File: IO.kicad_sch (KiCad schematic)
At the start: 17 parts, among them J701 Conn_01x02, J702 Raspberry_Pi_2_3

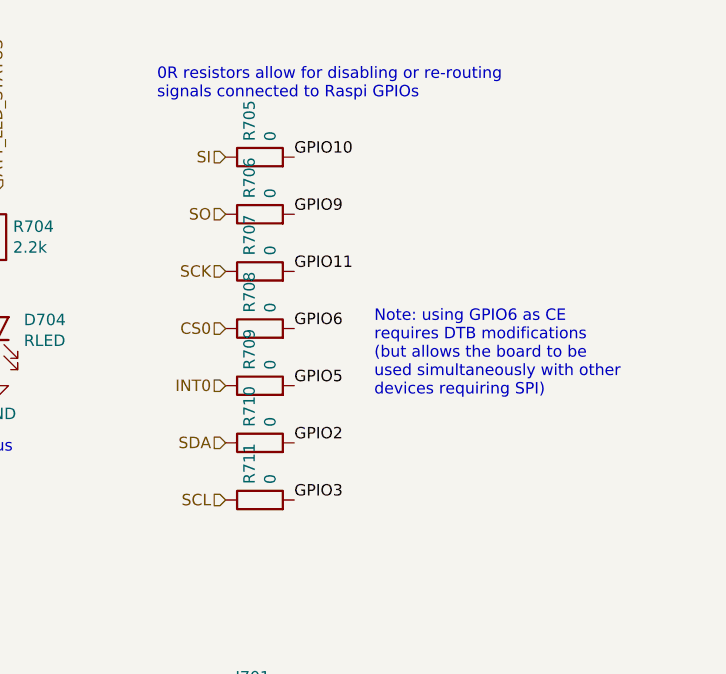
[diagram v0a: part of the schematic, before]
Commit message: Change the power supply topology
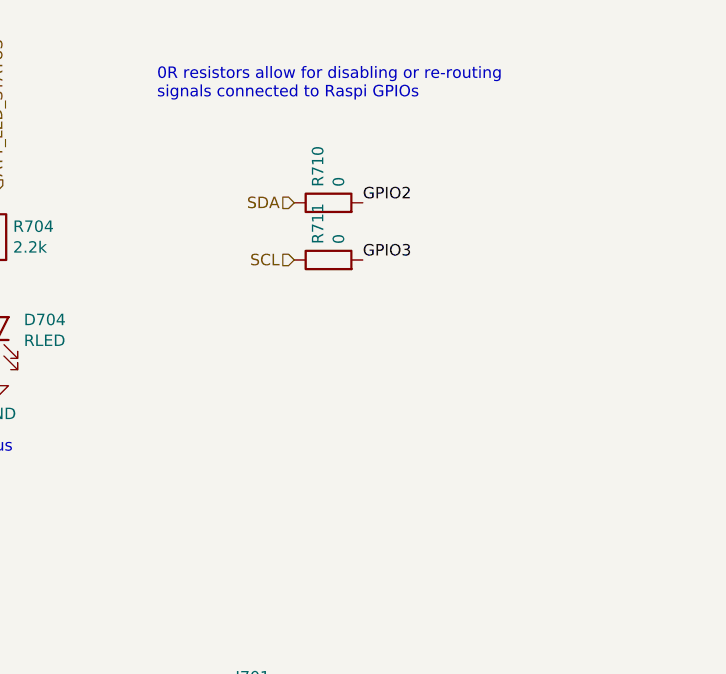
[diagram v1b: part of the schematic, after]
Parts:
- removed R705, R706, R707, R708, R709: 0, Resistor_SMD:R_0603_1608Metric, symbol Device:R
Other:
- note removed: "Note: using GPIO6 as CE requires DTB modifications (but allows the board to be used simultaneously with other devices requiring SPI)"
- moved on the sheet: R710, R711
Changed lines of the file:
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@@
-    (effects (font (size 1.27 1.27)) (justify left bottom))
-  )
-  (text "Note: using GPIO6 as CE\nrequires DTB modifications\n(but allows the board to be \nused simultaneously with other\ndevices requiring SPI)"
-    (at 184.15 63.5 0)
     (effects (font (size 1.27 1.27)) (justify left bottom))
   )
@@
     (effects (font (size 1.27 1.27)) (justify left bottom))
   )
-  (label "GPIO3" (at 175.26 74.93 0)
-    (effects (font (size 1.27 1.27)) (justify left bottom))
-  )
-  (label "GPIO6" (at 175.26 55.88 0)
-    (effects (font (size 1.27 1.27)) (justify left bottom))
-  )
-  (label "GPIO11" (at 175.26 49.53 0)
-    (effects (font (size 1.27 1.27)) (justify left bottom))
-  )
-  (label "GPIO5" (at 175.26 62.23 0)
+  (label "GPIO3" (at 182.88 48.26 0)
     (effects (font (size 1.27 1.27)) (justify left bottom))
   )
@@
     (effects (font (size 1.27 1.27)) (justify left bottom))
   )
-  (label "GPIO2" (at 175.26 68.58 0)
-    (effects (font (size 1.27 1.27)) (justify left bottom))
-  )
-  (label "GPIO9" (at 175.26 43.18 0)
-    (effects (font (size 1.27 1.27)) (justify left bottom))
-  )
-  (label "GPIO10" (at 175.26 36.83 0)
+  (label "GPIO2" (at 182.88 41.91 0)
     (effects (font (size 1.27 1.27)) (justify left bottom))
   )
@@
     (effects (font (size 1.27 1.27)) (justify left))
   )
-  (hierarchical_label "INT0" (shape input) (at 167.64 62.23 180)
-    (effects (font (size 1.27 1.27)) (justify right))
-  )
-  (hierarchical_label "SO" (shape input) (at 167.64 43.18 180)
-    (effects (font (size 1.27 1.27)) (justify right))
-  )
-  (hierarchical_label "SCL" (shape input) (at 167.64 74.93 180)
-    (effects (font (size 1.27 1.27)) (justify right))
-  )
-  (hierarchical_label "SI" (shape input) (at 167.64 36.83 180)
-    (effects (font (size 1.27 1.27)) (justify right))
-  )
-  (hierarchical_label "CS0" (shape input) (at 167.64 55.88 180)
+  (hierarchical_label "SCL" (shape input) (at 175.26 48.26 180)
     (effects (font (size 1.27 1.27)) (justify right))
   )
@@
     (effects (font (size 1.27 1.27)) (justify left))
   )
-  (hierarchical_label "SCK" (shape input) (at 167.64 49.53 180)
-    (effects (font (size 1.27 1.27)) (justify right))
-  )
-  (hierarchical_label "SDA" (shape input) (at 167.64 68.58 180)
+  (hierarchical_label "SDA" (shape input) (at 175.26 41.91 180)
     (effects (font (size 1.27 1.27)) (justify right))
   )
@@
     (pin "1")
   )
-  (symbol (lib_id "Device:R") (at 171.45 62.23 90) (unit 1)
-    (in_bom yes) (on_board yes)
-    (property "Reference" "R709" (id 0) (at 170.2816 60.452 0)
-      (effects (font (size 1.27 1.27)) (justify left))
-    )
-    (property "Value" "0" (id 1) (at 172.593 60.452 0)
-      (effects (font (size 1.27 1.27)) (justify left))
-    )
-    (property "Footprint" "Resistor_SMD:R_0603_1608Metric" (id 2) (at 171.45 64.008 90)
-      (effects (font (size 1.27 1.27)) hide)
-    )
-    (property "Datasheet" "~" (id 3) (at 171.45 62.23 0)
-      (effects (font (size 1.27 1.27)) hide)
-    )
-    (property "LCSC" "C21189" (id 4) (at 171.45 62.23 0)
-      (effects (font (size 1.27 1.27)) hide)
-    )
-    (pin "1")
-    (pin "2")
-  )
-  (symbol (lib_id "Device:R") (at 171.45 55.88 90) (unit 1)
-    (in_bom yes) (on_board yes)
-    (property "Reference" "R708" (id 0) (at 170.2816 54.102 0)
-      (effects (font (size 1.27 1.27)) (justify left))
-    )
-    (property "Value" "0" (id 1) (at 172.593 54.102 0)
-      (effects (font (size 1.27 1.27)) (justify left))
-    )
-    (property "Footprint" "Resistor_SMD:R_0603_1608Metric" (id 2) (at 171.45 57.658 90)
-      (effects (font (size 1.27 1.27)) hide)
-    )
-    (property "Datasheet" "~" (id 3) (at 171.45 55.88 0)
-      (effects (font (size 1.27 1.27)) hide)
-    )
-    (property "LCSC" "C21189" (id 4) (at 171.45 55.88 0)
-      (effects (font (size 1.27 1.27)) hide)
-    )
-    (pin "1")
-    (pin "2")
-  )
-  (symbol (lib_id "Device:R") (at 171.45 49.53 90) (unit 1)
-    (in_bom yes) (on_board yes)
-    (property "Reference" "R707" (id 0) (at 170.2816 47.752 0)
-      (effects (font (size 1.27 1.27)) (justify left))
-    )
-    (property "Value" "0" (id 1) (at 172.593 47.752 0)
-      (effects (font (size 1.27 1.27)) (justify left))
-    )
-    (property "Footprint" "Resistor_SMD:R_0603_1608Metric" (id 2) (at 171.45 51.308 90)
-      (effects (font (size 1.27 1.27)) hide)
-    )
-    (property "Datasheet" "~" (id 3) (at 171.45 49.53 0)
-      (effects (font (size 1.27 1.27)) hide)
-    )
-    (property "LCSC" "C21189" (id 4) (at 171.45 49.53 0)
-      (effects (font (size 1.27 1.27)) hide)
-    )
-    (pin "1")
-    (pin "2")
-  )
-  (symbol (lib_id "Device:R") (at 171.45 43.18 90) (unit 1)
-    (in_bom yes) (on_board yes)
-    (property "Reference" "R706" (id 0) (at 170.2816 41.402 0)
-      (effects (font (size 1.27 1.27)) (justify left))
-    )
-    (property "Value" "0" (id 1) (at 172.593 41.402 0)
-      (effects (font (size 1.27 1.27)) (justify left))
-    )
-    (property "Footprint" "Resistor_SMD:R_0603_1608Metric" (id 2) (at 171.45 44.958 90)
-      (effects (font (size 1.27 1.27)) hide)
-    )
-    (property "Datasheet" "~" (id 3) (at 171.45 43.18 0)
-      (effects (font (size 1.27 1.27)) hide)
-    )
-    (property "LCSC" "C21189" (id 4) (at 171.45 43.18 0)
-      (effects (font (size 1.27 1.27)) hide)
-    )
-    (pin "1")
-    (pin "2")
-  )
-  (symbol (lib_id "Device:R") (at 171.45 36.83 90) (unit 1)
-    (in_bom yes) (on_board yes)
-    (property "Reference" "R705" (id 0) (at 170.2816 35.052 0)
-      (effects (font (size 1.27 1.27)) (justify left))
-    )
-    (property "Value" "0" (id 1) (at 172.593 35.052 0)
-      (effects (font (size 1.27 1.27)) (justify left))
-    )
-    (property "Footprint" "Resistor_SMD:R_0603_1608Metric" (id 2) (at 171.45 38.608 90)
-      (effects (font (size 1.27 1.27)) hide)
-    )
-    (property "Datasheet" "~" (id 3) (at 171.45 36.83 0)
-      (effects (font (size 1.27 1.27)) hide)
-    )
-    (property "LCSC" "C21189" (id 4) (at 171.45 36.83 0)
-      (effects (font (size 1.27 1.27)) hide)
-    )
-    (pin "1")
-    (pin "2")
-  )
   (symbol (lib_id "Device:LED") (at 142.24 55.88 90) (unit 1)
     (in_bom yes) (on_board yes)
@@
     (pin "1")
   )
-  (symbol (lib_id "Device:R") (at 171.45 74.93 90) (unit 1)
-    (in_bom yes) (on_board yes)
-    (property "Reference" "R711" (id 0) (at 170.2816 73.152 0)
-      (effects (font (size 1.27 1.27)) (justify left))
-    )
-    (property "Value" "0" (id 1) (at 172.593 73.152 0)
-      (effects (font (size 1.27 1.27)) (justify left))
-    )
-    (property "Footprint" "Resistor_SMD:R_0603_1608Metric" (id 2) (at 171.45 76.708 90)
-      (effects (font (size 1.27 1.27)) hide)
-    )
-    (property "Datasheet" "~" (id 3) (at 171.45 74.93 0)
-      (effects (font (size 1.27 1.27)) hide)
-    )
-    (property "LCSC" "C21189" (id 4) (at 171.45 74.93 0)
-      (effects (font (size 1.27 1.27)) hide)
-    )
-    (pin "1")
-    (pin "2")
-  )
-  (symbol (lib_id "Device:R") (at 171.45 68.58 90) (unit 1)
-    (in_bom yes) (on_board yes)
-    (property "Reference" "R710" (id 0) (at 170.2816 66.802 0)
-      (effects (font (size 1.27 1.27)) (justify left))
-    )
-    (property "Value" "0" (id 1) (at 172.593 66.802 0)
-      (effects (font (size 1.27 1.27)) (justify left))
-    )
-    (property "Footprint" "Resistor_SMD:R_0603_1608Metric" (id 2) (at 171.45 70.358 90)
-      (effects (font (size 1.27 1.27)) hide)
-    )
-    (property "Datasheet" "~" (id 3) (at 171.45 68.58 0)
-      (effects (font (size 1.27 1.27)) hide)
-    )
-    (property "LCSC" "C21189" (id 4) (at 171.45 68.58 0)
-      (effects (font (size 1.27 1.27)) hide)
-    )
+  (symbol (lib_id "Device:R") (at 179.07 48.26 90) (unit 1)
+    (in_bom yes) (on_board yes)
+    (property "Reference" "R711" (id 0) (at 177.9016 46.482 0)
+      (effects (font (size 1.27 1.27)) (justify left))
+    )
+    (property "Value" "0" (id 1) (at 180.213 46.482 0)
+      (effects (font (size 1.27 1.27)) (justify left))
+    )
+    (property "Footprint" "Resistor_SMD:R_0603_1608Metric" (id 2) (at 179.07 50.038 90)
+      (effects (font (size 1.27 1.27)) hide)
+    )
+    (property "Datasheet" "~" (id 3) (at 179.07 48.26 0)
+      (effects (font (size 1.27 1.27)) hide)
+    )
+    (property "LCSC" "C21189" (id 4) (at 179.07 48.26 0)
+      (effects (font (size 1.27 1.27)) hide)
+    )
+    (pin "1")
+    (pin "2")
+  )
+  (symbol (lib_id "Device:R") (at 179.07 41.91 90) (unit 1)
+    (in_bom yes) (on_board yes)
+    (property "Reference" "R710" (id 0) (at 177.9016 40.132 0)
+      (effects (font (size 1.27 1.27)) (justify left))
+    )
+    (property "Value" "0" (id 1) (at 180.213 40.132 0)
+      (effects (font (size 1.27 1.27)) (justify left))
+    )
+    (property "Footprint" "Resistor_SMD:R_0603_1608Metric" (id 2) (at 179.07 43.688 90)
+      (effects (font (size 1.27 1.27)) hide)
+    )
+    (property "Datasheet" "~" (id 3) (at 179.07 41.91 0)
+      (effects (font (size 1.27 1.27)) hide)
+    )
+    (property "LCSC" "C21189" (id 4) (at 179.07 41.91 0)
+      (effects (font (size 1.27 1.27)) hide)
+    )

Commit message: SH-RPi v2 schematic design
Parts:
- removed D702, D704: RLED, LED_SMD:LED_0603_1608Metric, symbol Device:LED
- removed D703: GLED, LED_SMD:LED_0603_1608Metric, symbol Device:LED
- removed R702, R703, R704: 2.2k, Resistor_SMD:R_0402_1005Metric, symbol Device:R
- removed R710, R711: 0, Resistor_SMD:R_0603_1608Metric, symbol Device:R
- added D501, D502, D503, D505, D507: ESD5451N, Diode_SMD:D_0402_1005Metric, symbol Device:D_TVS
- added D504, D506: 1N5819WS, Diode_SMD:D_SOD-323, symbol Device:D_Schottky
- added D509, D510, D511: WHITE LED, LED_SMD:LED_0603_1608Metric, symbol Device:LED
- added J502: Conn_01x02, symbol Connector_Generic:Conn_01x02
- added R502, R503, R504: 1.0k, Resistor_SMD:R_0402_1005Metric, symbol Device:R
- D508: renamed from D701; value GLED -> WHITE LED; LCSC C72043 -> C434422
- J503: renamed from J701; footprint Connector_PinHeader_2.54mm:PinHeader_1x02_P2.54mm_Vertical -> (none)
- R501: renamed from R701; value 2.2k -> 1.0k; LCSC C25879 -> (none)
- renumbered J702 to J501
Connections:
- net GPIO2 is gone; now on net SDA: J501.3 (SDA/GPIO2)
- net GPIO3 is gone; now on net SCL: J501.5 (SCL/GPIO3)
- net +3V3: now also D501.2 (A2), D504.1 (K), D506.1 (K); no longer J501.1 (3V3), J501.17 (3V3)
- net 5V: now also J503.1 (Pin_1), D502.2 (A2), D503.2 (A2), J502.1 (Pin_1); no longer J501.2 (5V), J501.4 (5V), J503.2 (Pin_2)
- net GND: now also J503.2 (Pin_2), D501.1 (A1), D502.1 (A1), D503.1 (A1), D505.1 (A1), D507.1 (A1), D509.1 (K), D510.1 (K), D511.1 (K), J502.2 (Pin_2); no longer J503.1 (Pin_1)
- net SCL: now also D506.2 (A), D507.2 (A2)
- net SDA: now also D504.2 (A), D505.2 (A2)
- net RXD0: now reaches J501.10 (GPIO15/RXD)
- net TXD5: now reaches J501.32 (PWM0/GPIO12)
- net RXD5: now reaches J501.33 (PWM1/GPIO13)
- net TXD0: now reaches J501.8 (GPIO14/TXD)
- net ATT_LED_VIN renamed LED_1
- net GPIO10: no longer names the net of J501.19 (MOSI0/GPIO10)
- net GPIO11: no longer names the net of J501.23 (SCLK0/GPIO11)
- net GPIO5: no longer names the net of J501.29 (GCLK1/GPIO5)
- net GPIO6: no longer names the net of J501.31 (GCLK2/GPIO6)
- net GPIO9: no longer names the net of J501.21 (MISO0/GPIO9)
- new net: D511.2 (A), R504.2
- new net: D510.2 (A), R503.2
- new net: D509.2 (A), R502.2
- new net +3.3V: J501.1 (3V3), J501.17 (3V3)
- new net +5V: J501.2 (5V), J501.4 (5V)
- new net LED_2: R502.1
- new net LED_3: R503.1
- new net LED_4: R504.1
- no-connect marks 21 -> 22
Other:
- note added: "5V power output"
- note added: "External connectors"
- note added: "Extra connector for 5V output for fans and similar."
- note added: "Protection for externally connected I2C"
- note removed: "0R resistors allow for disabling or re-routing signals connected to Raspi GPIOs"
- note removed: "5V enabled"
- note removed: "Extra header connector for 5V output for fans and similar."
- note removed: "Status"
- note removed: "Vcap"
- note removed: "Vin voltage"
- moved on the sheet: D508, J503, R501

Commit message: WIP: Assign footprints and LCSC part numbers
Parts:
- J501: footprint SH-RPi:PinHeader_RPi-GPIO -> SH-RPi:PassthroughPinSocket_2x40_P2.54mm_Vertical; LCSC (none) -> C2685115
- J502: footprint (none) -> Connector_Phoenix_MC:PhoenixContact_MC_1,5_2-G-3.81_1x02_P3.81mm_Horizontal
- J503: footprint (none) -> Connector_JST:JST_XH_S2B-XH-A_1x02_P2.50mm_Horizontal
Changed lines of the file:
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@@
     (property "Reference" "J501" (id 0) (at 67.31 40.64 0))
     (property "Value" "Raspberry_Pi_2_3" (id 1) (at 74.93 43.18 0))
-    (property "Footprint" "SH-RPi:PinHeader_RPi-GPIO" (id 2) (at 59.69 76.2 0)
+    (property "Footprint" "SH-RPi:PassthroughPinSocket_2x40_P2.54mm_Vertical" (id 2) (at 59.69 76.2 0)
       (effects (font (size 1.27 1.27)) hide)
     )
     (property "Datasheet" "https://www.raspberrypi.org/documentation/hardware/raspberrypi/schematics/rpi_SCH_3bplus_1p0_reduced.pdf" (id 3) (at 59.69 76.2 0)
+      (effects (font (size 1.27 1.27)) hide)
+    )
+    (property "LCSC" "C2685115" (id 4) (at 59.69 76.2 0)
       (effects (font (size 1.27 1.27)) hide)
     )
@@
     (property "Reference" "J503" (id 0) (at 169.3672 146.685 0))
     (property "Value" "Conn_01x02" (id 1) (at 169.3672 144.3736 0))
-    (property "Footprint" "" (id 2) (at 171.45 138.43 0)
+    (property "Footprint" "Connector_JST:JST_XH_S2B-XH-A_1x02_P2.50mm_Horizontal" (id 2) (at 171.45 138.43 0)
       (effects (font (size 1.27 1.27)) hide)
     )
@@
     (property "Reference" "J502" (id 0) (at 169.3672 123.825 0))
     (property "Value" "Conn_01x02" (id 1) (at 169.3672 121.5136 0))
-    (property "Footprint" "" (id 2) (at 171.45 115.57 0)
-      (effects (font (size 1.27 1.27)) hide)
-    )
+    (property "Footprint" "Connector_Phoenix_MC:PhoenixContact_MC_1,5_2-G-3.81_1x02_P3.81mm_Horizontal" (id 2) (at 171.45 115.57 0)
+      (effects (font (size 1.27 1.27)) hide)
+    )

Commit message: Assign footprints and part numbers to components
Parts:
- J502: LCSC (none) -> C8387
- J503: LCSC (none) -> C33132
- R501, R502, R503, R504: value 1.0k -> 1k; LCSC (none) -> C11702
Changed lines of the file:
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@@
       (effects (font (size 1.27 1.27)) (justify left))
     )
-    (property "Value" "1.0k" (id 1) (at 221.488 51.943 0)
+    (property "Value" "1k" (id 1) (at 221.488 51.943 0)
       (effects (font (size 1.27 1.27)) (justify left))
     )
@@
       (effects (font (size 1.27 1.27)) hide)
     )
-    (property "LCSC" "" (id 4) (at 219.71 50.8 0)
+    (property "LCSC" "C11702" (id 4) (at 219.71 50.8 0)
       (effects (font (size 1.27 1.27)) hide)
     )
@@
       (effects (font (size 1.27 1.27)) hide)
     )
+    (property "LCSC" "C33132" (id 4) (at 171.45 138.43 0)
+      (effects (font (size 1.27 1.27)) hide)
+    )
     (pin "1")
     (pin "2")
@@
       (effects (font (size 1.27 1.27)) hide)
     )
+    (property "LCSC" "C8387" (id 4) (at 171.45 115.57 0)
+      (effects (font (size 1.27 1.27)) hide)
+    )
     (pin "1")
     (pin "2")
@@
       (effects (font (size 1.27 1.27)) (justify left))
     )
-    (property "Value" "1.0k" (id 1) (at 267.208 51.943 0)
+    (property "Value" "1k" (id 1) (at 267.208 51.943 0)
       (effects (font (size 1.27 1.27)) (justify left))
     )
@@
       (effects (font (size 1.27 1.27)) hide)
     )
-    (property "LCSC" "" (id 4) (at 265.43 50.8 0)
+    (property "LCSC" "C11702" (id 4) (at 265.43 50.8 0)
       (effects (font (size 1.27 1.27)) hide)
     )
@@
       (effects (font (size 1.27 1.27)) (justify left))
     )
-    (property "Value" "1.0k" (id 1) (at 251.968 51.943 0)
+    (property "Value" "1k" (id 1) (at 251.968 51.943 0)
       (effects (font (size 1.27 1.27)) (justify left))
     )
@@
       (effects (font (size 1.27 1.27)) hide)
     )
-    (property "LCSC" "" (id 4) (at 250.19 50.8 0)
+    (property "LCSC" "C11702" (id 4) (at 250.19 50.8 0)
       (effects (font (size 1.27 1.27)) hide)
     )
@@
       (effects (font (size 1.27 1.27)) (justify left))
     )
-    (property "Value" "1.0k" (id 1) (at 236.728 51.943 0)
+    (property "Value" "1k" (id 1) (at 236.728 51.943 0)
       (effects (font (size 1.27 1.27)) (justify left))
     )
@@
       (effects (font (size 1.27 1.27)) hide)
     )
-    (property "LCSC" "" (id 4) (at 234.95 50.8 0)
-      (effects (font (size 1.27 1.27)) hide)
-    )
+    (property "LCSC" "C11702" (id 4) (at 234.95 50.8 0)
+      (effects (font (size 1.27 1.27)) hide)
+    )

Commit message: Initial PCB component layout done
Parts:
- J503: footprint Connector_JST:JST_XH_S2B-XH-A_1x02_P2.50mm_Horizontal -> SH-RPi:Boomelec_XH-2AW_1x02_P2.50mm_Horiz
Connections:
- net L1_: now reaches D508.2 (A), R501.2
- net L4_: now reaches D511.2 (A), R504.2
- net L3_: now reaches D510.2 (A), R503.2
- net L2_: now reaches D509.2 (A), R502.2
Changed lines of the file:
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@@
+    (effects (font (size 1.27 1.27)) (justify left bottom))
+  )
+  (label "L2_" (at 234.95 55.88 0)
+    (effects (font (size 1.27 1.27)) (justify left bottom))
+  )
+  (label "L1_" (at 219.71 55.88 0)
+    (effects (font (size 1.27 1.27)) (justify left bottom))
+  )
+  (label "L4_" (at 265.43 55.88 0)
+    (effects (font (size 1.27 1.27)) (justify left bottom))
+  )
+  (label "L3_" (at 250.19 55.88 0)
     (effects (font (size 1.27 1.27)) (justify left bottom))
   )
@@
     (property "Reference" "J503" (id 0) (at 169.3672 146.685 0))
     (property "Value" "Conn_01x02" (id 1) (at 169.3672 144.3736 0))
-    (property "Footprint" "Connector_JST:JST_XH_S2B-XH-A_1x02_P2.50mm_Horizontal" (id 2) (at 171.45 138.43 0)
-      (effects (font (size 1.27 1.27)) hide)
-    )
+    (property "Footprint" "SH-RPi:Boomelec_XH-2AW_1x02_P2.50mm_Horiz" (id 2) (at 171.45 138.43 0)
+      (effects (font (size 1.27 1.27)) hide)
+    )
